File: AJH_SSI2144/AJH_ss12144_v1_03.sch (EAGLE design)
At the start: 57 parts, among them IC1 LM4040 5.0V, IC2 TL074D, IC3 TL072D, J100 PJ301_THONKICONN6, J101 PJ301_THONKICONN6, J102 PJ301_THONKICONN6, J103 PJ301_THONKICONN6, U1 BCM847BS

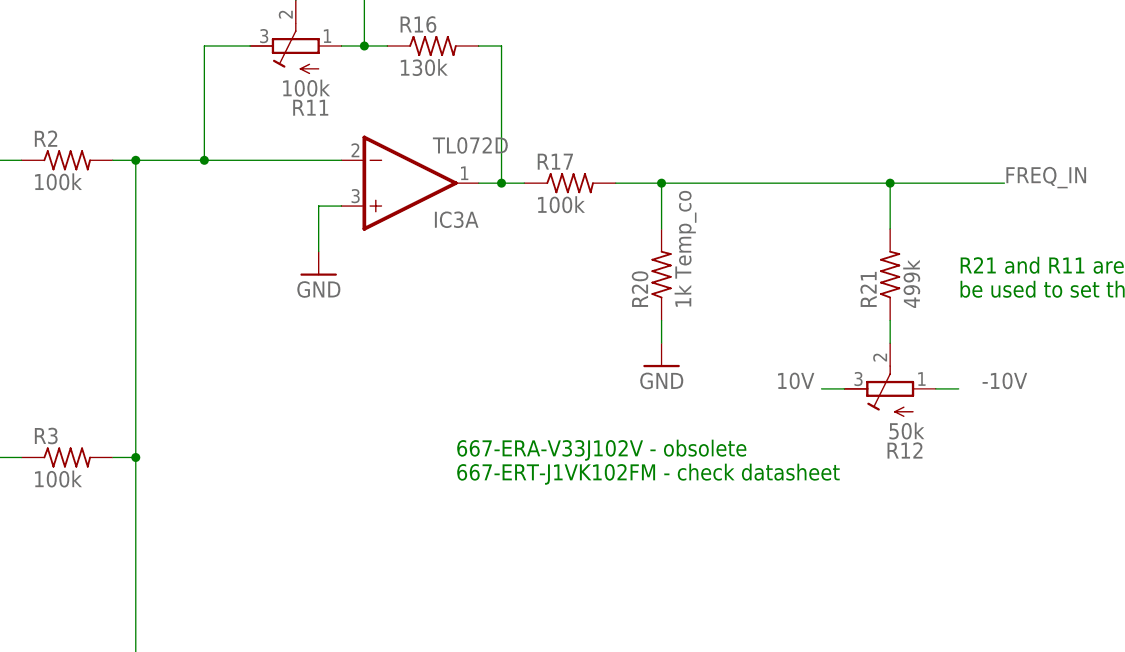
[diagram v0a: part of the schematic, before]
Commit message: Add through hole tempco to ssi2144
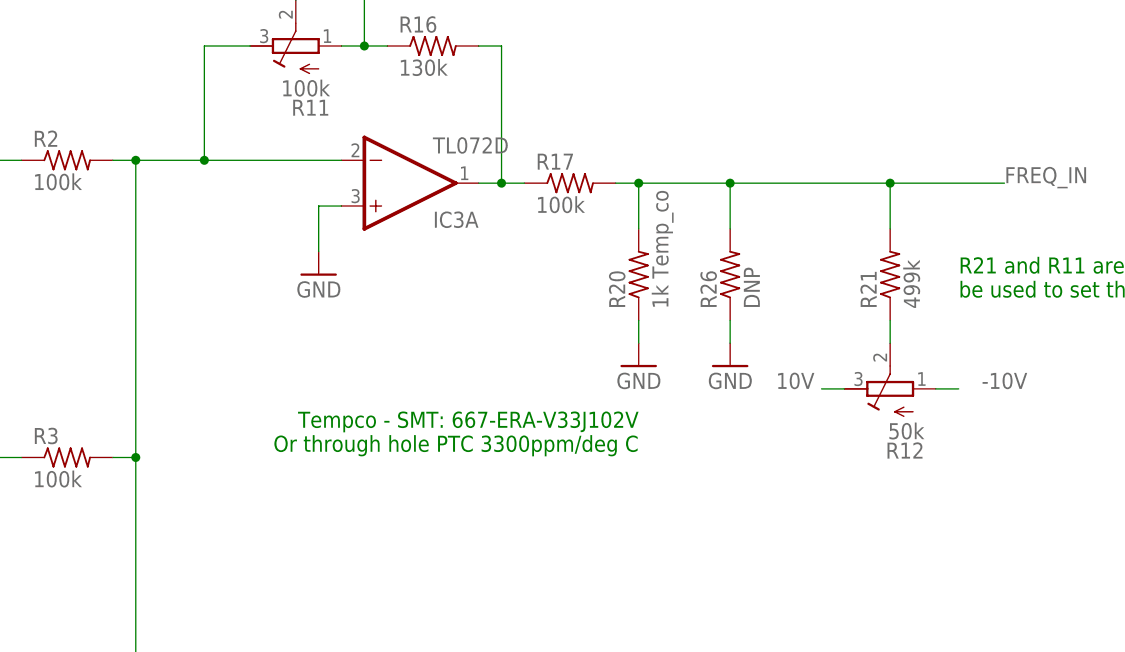
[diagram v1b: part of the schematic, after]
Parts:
- added R26: DNP, rcl:R-US_0204/7
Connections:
- net FREQ_IN: now also R26.2
- net GND: now also R26.1
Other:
- note added: "Tempco - SMT: 667-ERA-V33J102V Or through hole PTC 3300ppm/deg C"
- note removed: "667-ERA-V33J102V - obsolete 667-ERT-J1VK102FM - check datasheet"
- moved on the sheet: R20
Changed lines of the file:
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@@
 <part name="GND15" library="SparkFun" deviceset="GND" device=""/>
 <part name="C16" library="rcl" deviceset="C-US" device="C0603" value="3.3n"/>
+<part name="R26" library="rcl" deviceset="R-US_" device="0204/7" value="DNP"/>
+<part name="GND4" library="SparkFun" deviceset="GND" device=""/>
 </parts>
 <sheets>
@@
 <plain>
 <text x="-114.3" y="-137.16" size="1.778" layer="94">+</text>
-<text x="-109.22" y="-60.96" size="1.778" layer="91">667-ERA-V33J102V - obsolete
-667-ERT-J1VK102FM - check datasheet</text>
+<text x="-88.9" y="-53.34" size="1.778" layer="91" rot="R180">Tempco - SMT: 667-ERA-V33J102V
+Or through hole PTC 3300ppm/deg C</text>
 <text x="-142.24" y="-2.54" size="1.778" layer="91">SSI2144 needs ~ -19mv/oct, but parts have quite wide variability
 So choose either R11=100k and R16=130k; or  R11=50k and R16=162k</text>
@@
 <attribute name="VALUE" x="-57.658" y="-41.91" size="1.778" layer="96" rot="R90"/>
 </instance>
-<instance part="R20" gate="G$1" x="-86.36" y="-38.1" smashed="yes" rot="R90">
-<attribute name="NAME" x="-87.8586" y="-41.91" size="1.778" layer="95" rot="R90"/>
-<attribute name="VALUE" x="-83.058" y="-41.91" size="1.778" layer="96" rot="R90"/>
-</instance>
-<instance part="GND15" gate="1" x="-86.36" y="-48.26" smashed="yes" rot="MR0">
-<attribute name="VALUE" x="-83.82" y="-50.8" size="1.778" layer="96" rot="MR0"/>
+<instance part="R20" gate="G$1" x="-88.9" y="-38.1" smashed="yes" rot="R90">
+<attribute name="NAME" x="-90.3986" y="-41.91" size="1.778" layer="95" rot="R90"/>
+<attribute name="VALUE" x="-85.598" y="-41.91" size="1.778" layer="96" rot="R90"/>
+</instance>
+<instance part="GND15" gate="1" x="-88.9" y="-48.26" smashed="yes" rot="MR0">
+<attribute name="VALUE" x="-86.36" y="-50.8" size="1.778" layer="96" rot="MR0"/>
 </instance>
 <instance part="C16" gate="G$1" x="12.7" y="35.56" smashed="yes" rot="R90">
 <attribute name="NAME" x="12.065" y="36.576" size="1.778" layer="95" rot="R90"/>
 <attribute name="VALUE" x="16.891" y="36.576" size="1.778" layer="96" rot="R90"/>
+</instance>
+<instance part="R26" gate="G$1" x="-78.74" y="-38.1" smashed="yes" rot="R90">
+<attribute name="NAME" x="-80.2386" y="-41.91" size="1.778" layer="95" rot="R90"/>
+<attribute name="VALUE" x="-75.438" y="-41.91" size="1.778" layer="96" rot="R90"/>
+</instance>
+<instance part="GND4" gate="1" x="-78.74" y="-48.26" smashed="yes" rot="MR0">
+<attribute name="VALUE" x="-76.2" y="-50.8" size="1.778" layer="96" rot="MR0"/>
 </instance>
 </instances>
@@
 <pinref part="R20" gate="G$1" pin="1"/>
 <pinref part="GND15" gate="1" pin="GND"/>
-<wire x1="-86.36" y1="-43.18" x2="-86.36" y2="-45.72" width="0.1524" layer="91"/>
+<wire x1="-88.9" y1="-43.18" x2="-88.9" y2="-45.72" width="0.1524" layer="91"/>
+</segment>
+<segment>
+<pinref part="R26" gate="G$1" pin="1"/>
+<pinref part="GND4" gate="1" pin="GND"/>
+<wire x1="-78.74" y1="-43.18" x2="-78.74" y2="-45.72" width="0.1524" layer="91"/>
 </segment>
 </net>
@@
 <segment>
 <pinref part="R17" gate="G$1" pin="2"/>
-<wire x1="-91.44" y1="-27.94" x2="-86.36" y2="-27.94" width="0.1524" layer="91"/>
+<wire x1="-91.44" y1="-27.94" x2="-88.9" y2="-27.94" width="0.1524" layer="91"/>
 <label x="-48.26" y="-27.94" size="1.778" layer="95"/>
-<wire x1="-86.36" y1="-27.94" x2="-60.96" y2="-27.94" width="0.1524" layer="91"/>
+<wire x1="-88.9" y1="-27.94" x2="-78.74" y2="-27.94" width="0.1524" layer="91"/>
+<wire x1="-78.74" y1="-27.94" x2="-60.96" y2="-27.94" width="0.1524" layer="91"/>
 <wire x1="-60.96" y1="-27.94" x2="-48.26" y2="-27.94" width="0.1524" layer="91"/>
-<wire x1="-86.36" y1="-27.94" x2="-86.36" y2="-33.02" width="0.1524" layer="91"/>
-<junction x="-86.36" y="-27.94"/>
+<wire x1="-88.9" y1="-27.94" x2="-88.9" y2="-33.02" width="0.1524" layer="91"/>
+<junction x="-88.9" y="-27.94"/>
 <pinref part="R20" gate="G$1" pin="2"/>
 <pinref part="R21" gate="G$1" pin="2"/>
 <wire x1="-60.96" y1="-33.02" x2="-60.96" y2="-27.94" width="0.1524" layer="91"/>
 <junction x="-60.96" y="-27.94"/>
-</segment>
-<segment>
+<pinref part="R26" gate="G$1" pin="2"/>
+<wire x1="-78.74" y1="-33.02" x2="-78.74" y2="-27.94" width="0.1524" layer="91"/>
+<junction x="-78.74" y="-27.94"/>
+</segment>
+<segment>

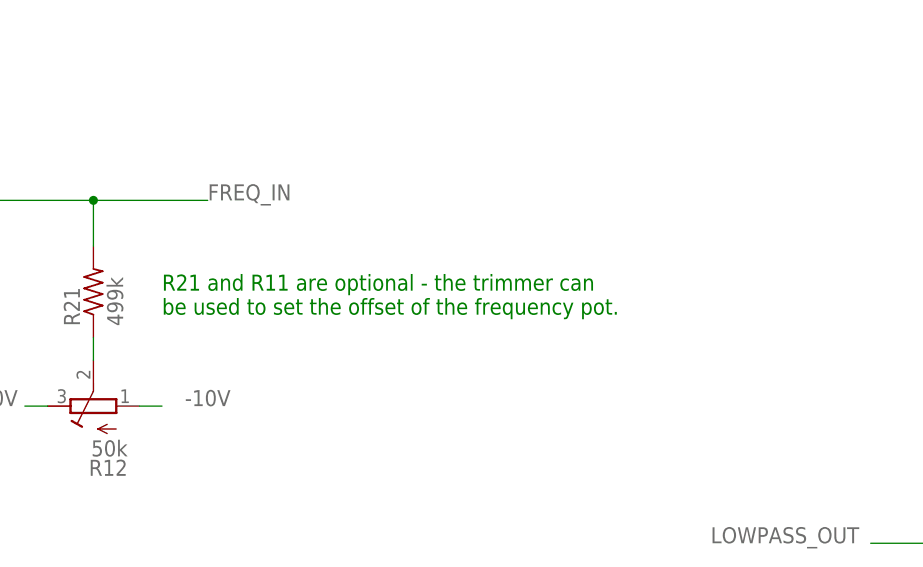
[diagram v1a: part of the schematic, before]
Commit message: Typo on ssi2144 schematic comments
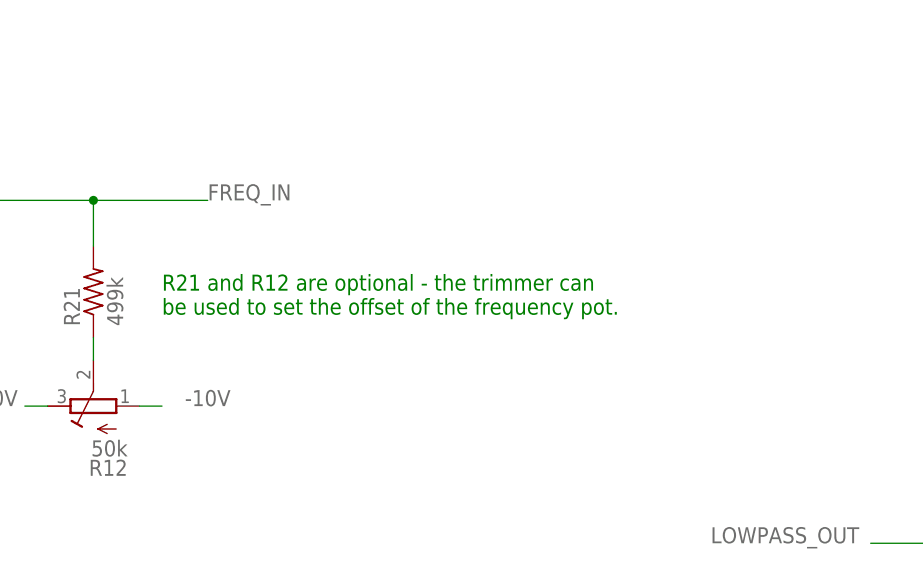
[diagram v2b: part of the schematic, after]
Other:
- note added: "R21 and R12 are optional - the trimmer can be used to set the offset of the frequency pot."
- note removed: "R21 and R11 are optional - the trimmer can be used to set the offset of the frequency pot."
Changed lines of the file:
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@@
 <text x="-142.24" y="-2.54" size="1.778" layer="91">SSI2144 needs ~ -19mv/oct, but parts have quite wide variability
 So choose either R11=100k and R16=130k; or  R11=50k and R16=162k</text>
-<text x="-53.34" y="-40.64" size="1.778" layer="91">R21 and R11 are optional - the trimmer can
+<text x="-53.34" y="-40.64" size="1.778" layer="91">R21 and R12 are optional - the trimmer can
 be used to set the offset of the frequency pot.</text>
 </plain>
